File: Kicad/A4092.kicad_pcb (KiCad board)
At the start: 4 copper layers, 175.6 x 122.1 mm, 118 parts, among them CN1 Zorro3, J1 Conn_02x25_Odd_Even, J2 Conn_01x06_Pin, J3 TO-LED, J4 TO-MB, J5 Conn_02x25_Odd_Even, J7 22112042, J8 TO-A3000-LED, J9 TO-A3000-MB, SW1 219-8MST, U1 SN74ABT16543DGGR, U10 NCR53c710 SCSI Host Controller, U11 DS21S07A, U12 DS21S07A, U13 SST39SF010/020/040, U2 SN74ABT16543DGGR, U3 SN74ABT16543DGGR, U4 SN74ABT16543DGGR, U5 74LVC07APW_118, U6 SN74ABT16245ADGGR, U7 AMS1117-3.3, U8 SN74F244DB, U9 XC95144XL-TQ144, Y1 Abracon ACO-50MHz

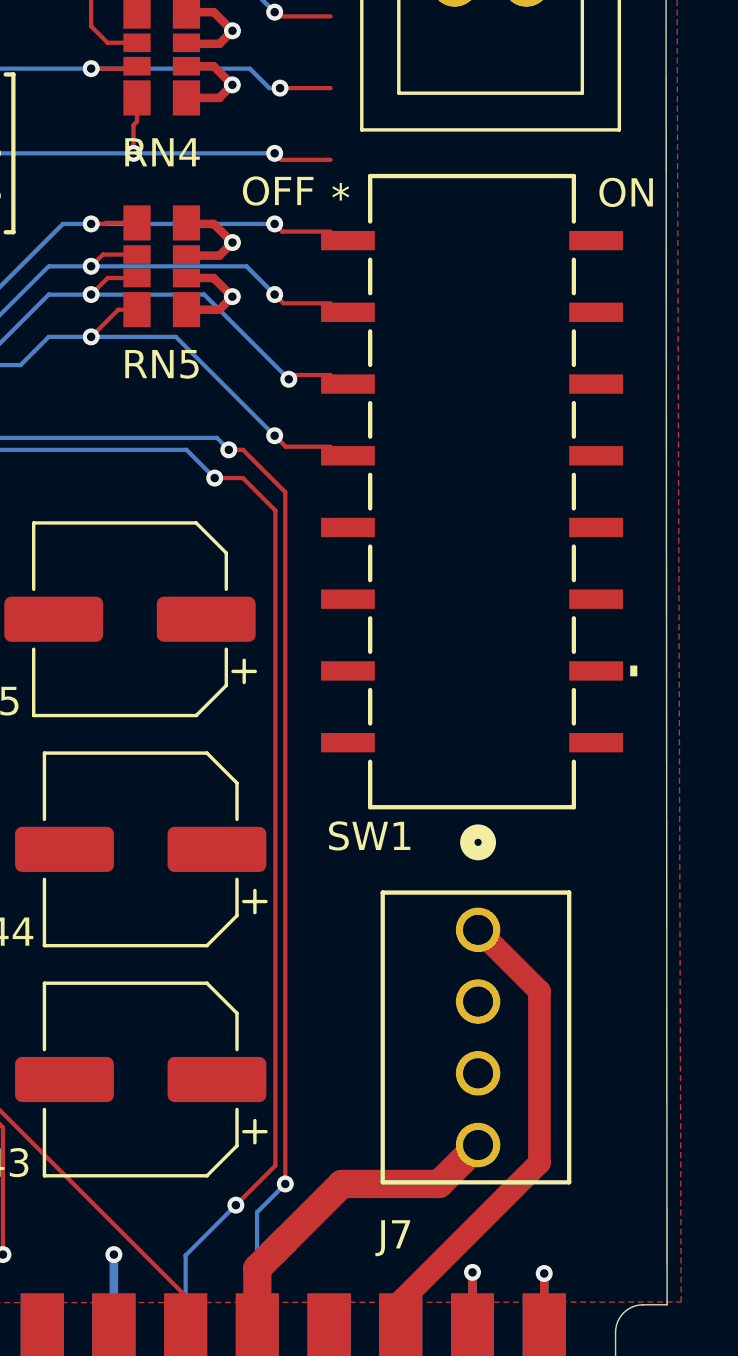
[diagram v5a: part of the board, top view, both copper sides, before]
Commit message: Fix up molex connector
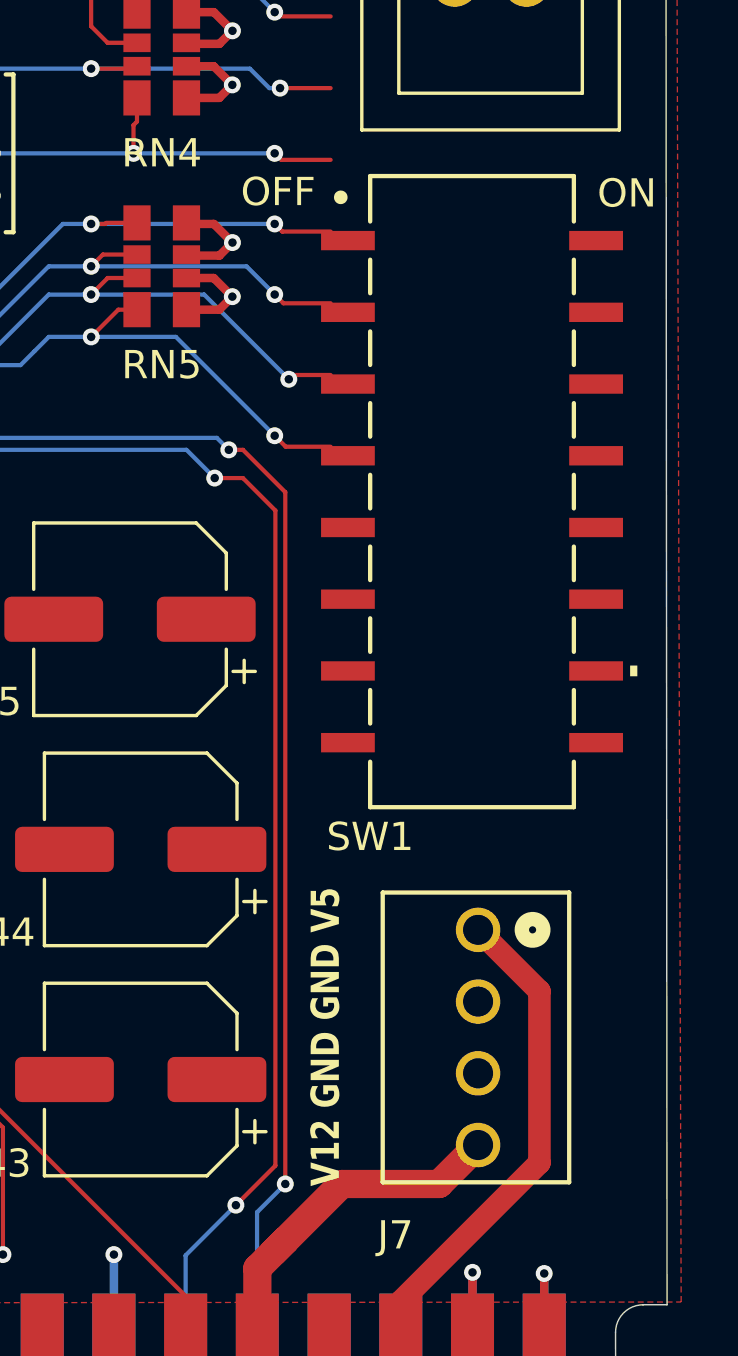
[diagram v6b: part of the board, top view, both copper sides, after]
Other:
- board text added: "V12 GND GND V5"
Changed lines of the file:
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@@
 		)
 		(fp_circle
-			(center -3.0988 0)
-			(end -2.7178 0)
+			(center 0 -1.93)
+			(end 0.381 -1.93)
 			(stroke
 				(width 0.508)
@@
 			(layer "F.SilkS")
 		)
-		(fp_circle
-			(center -3.0988 0)
-			(end -2.7178 0)
-			(stroke
-				(width 0.508)
-				(type solid)
-			)
-			(fill no)
-			(layer "B.SilkS")
-		)
 		(fp_line
 			(start -1.4478 3.504001)
@@
 		)
 		(embedded_fonts no)
-		(model "${KIPRJMOD}/Libraries/022112042.stp"
-			(offset
-				(xyz 3.7 0 0)
-			)
-			(scale
-				(xyz 1 1 1)
-			)
-			(rotate
-				(xyz -90 -0 -0)
-			)
-		)
 	)
 	(footprint "Capacitor_SMD:C_0603_1608Metric_Pad1.08x0.95mm_HandSolder"
@@
 			)
 		)
-		(fp_text user "*"
-			(at -4.6482 -10.3759 0)
-			(layer "F.SilkS")
-			(effects
-				(font
-					(size 1 1)
-					(thickness 0.15)
-				)
-			)
-		)
 		(fp_text user "OFF"
 			(at -6.8628 -10.61 0)
@@
 			)
 		)
-		(fp_text user "*"
+		(fp_text user "•"
 			(at -4.6482 -10.3759 0)
 			(unlocked yes)
@@
 				(font
 					(size 1 1)
-					(thickness 0.15)
+					(thickness 0.2)
+					(bold yes)
 				)
 			)
@@
 			)
 			(justify left bottom)
+		)
+	)
+	(gr_text "V12 GND GND V5"
+		(at 213.02 143.08 90)
+		(layer "F.SilkS")
+		(effects
+			(font
+				(size 1 0.8)
+				(thickness 0.2)
+				(bold yes)
+			)
+			(justify left bottom)

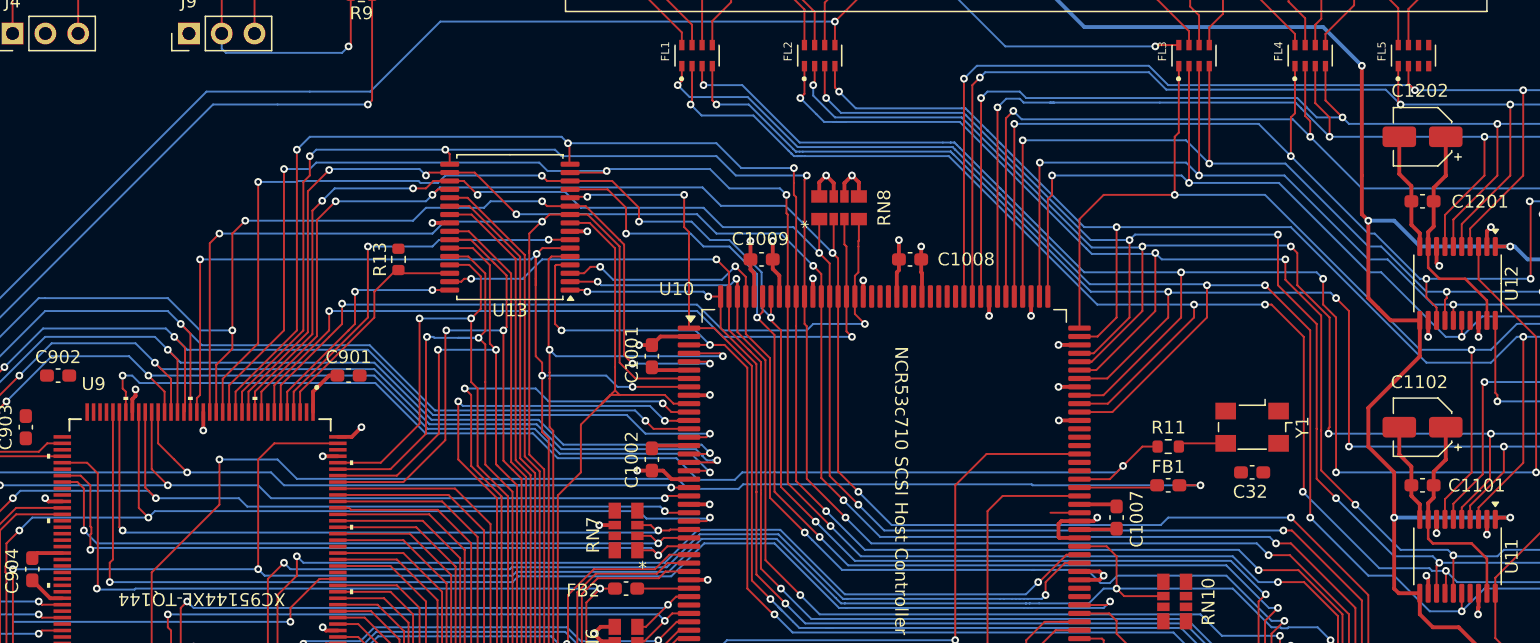
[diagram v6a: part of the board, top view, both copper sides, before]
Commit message: Update termination capacitors to tantalum
and clean up bypass caps in schematic
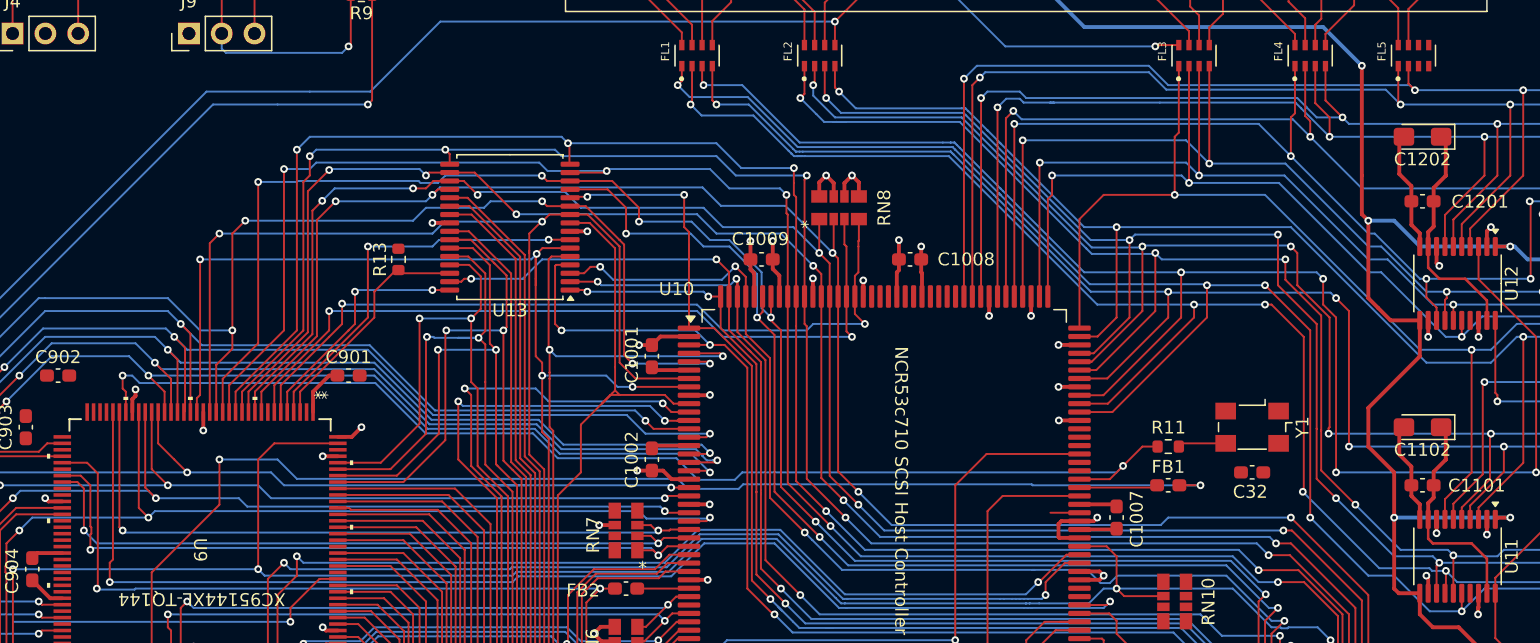
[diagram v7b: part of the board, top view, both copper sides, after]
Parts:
- C1102, C1202: footprint Capacitor_SMD:CP_Elec_4x5.7 -> Capacitor_Tantalum_SMD:CP_EIA-3216-10_Kemet-I_HandSolder
